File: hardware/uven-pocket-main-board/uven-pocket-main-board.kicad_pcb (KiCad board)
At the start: 4 copper layers, 120 x 56 mm, 78 parts, among them J1 Raspberry_Pi_2_3, J10 VDrive, J11 GND, J2 FAN, J3 TEMP_CHAMBER1, J4 TEMP_CHAMBER0, J5 1-282834-2, J6 VDrive, J7 GND, J8 VDrive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

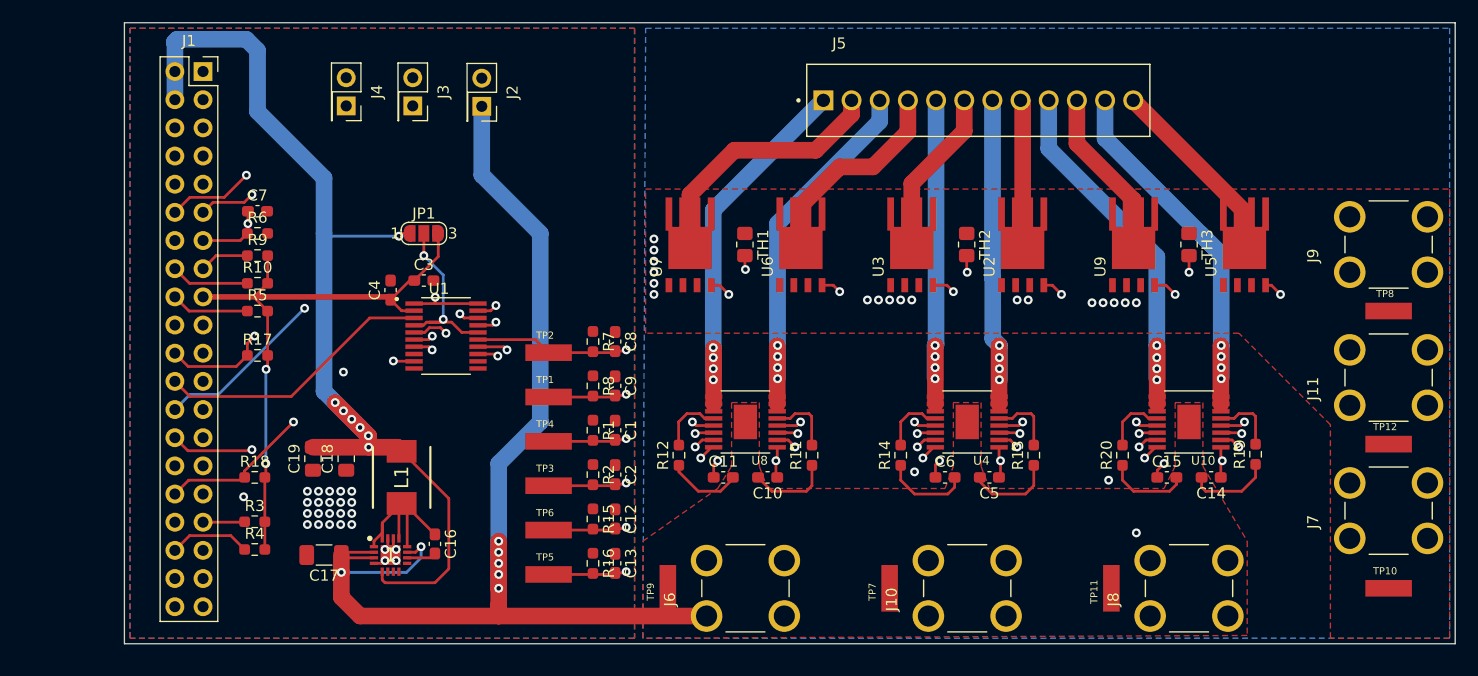
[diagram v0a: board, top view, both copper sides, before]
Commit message: single led copper base + uven pocket finished
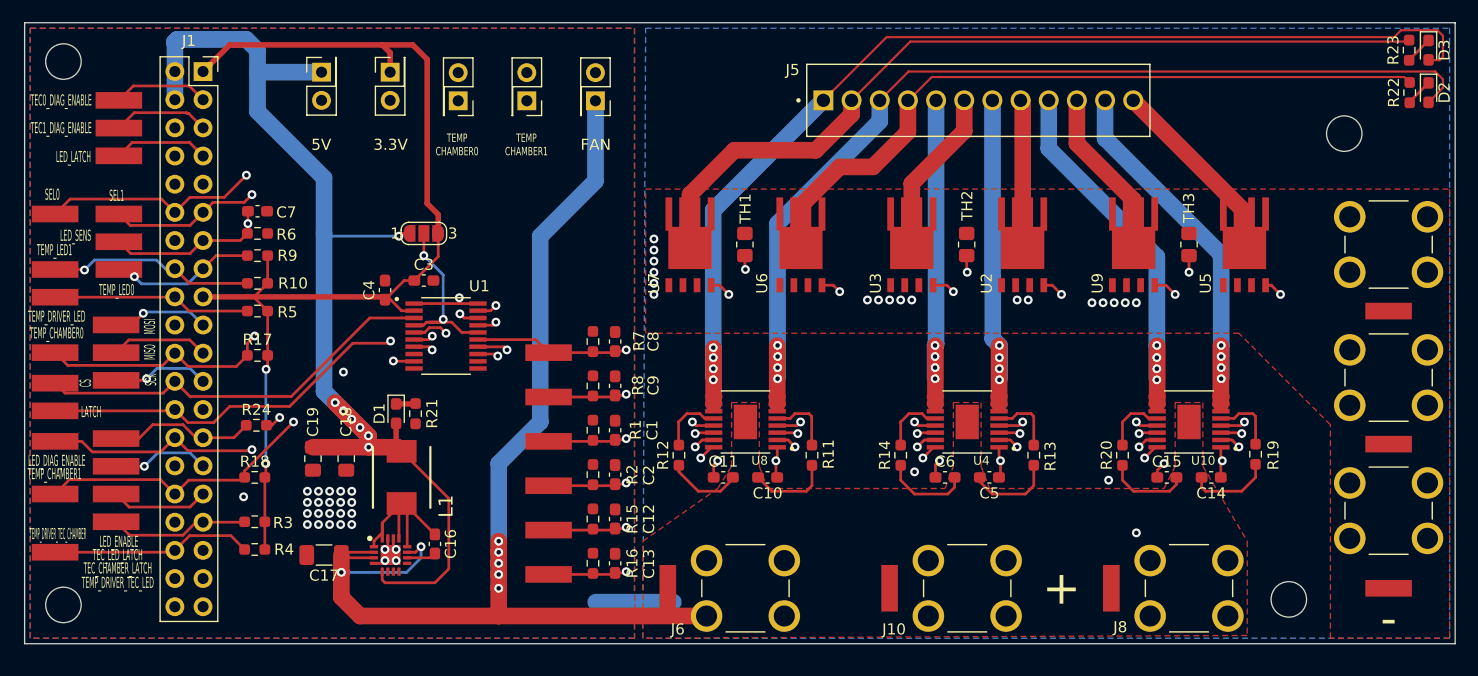
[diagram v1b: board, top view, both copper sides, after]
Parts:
- added D1: LED, LED_SMD:LED_0603_1608Metric_Pad1.05x0.95mm_HandSolder, F.Cu at (136.5, 92.2)
- added D2: LED, LED_SMD:LED_0603_1608Metric_Pad1.05x0.95mm_HandSolder, F.Cu at (229.6, 63.3)
- added D3: LED, LED_SMD:LED_0603_1608Metric_Pad1.05x0.95mm_HandSolder, F.Cu at (229.6, 59.5)
- added H1: MountingHole, MountingHole:MountingHole_3.2mm_M3, F.Cu at (217.0, 109.0)
- added H2: MountingHole, MountingHole:MountingHole_3.2mm_M3, F.Cu at (106.5, 109.5)
- added H3: MountingHole, MountingHole:MountingHole_3.2mm_M3, F.Cu at (106.5, 60.5)
- added H4: MountingHole, MountingHole:MountingHole_3.2mm_M3, F.Cu at (222.0, 67.0)
- added J12: 3.3V, Connector_PinSocket_2.54mm:PinSocket_2x01_P2.54mm_Vertical, F.Cu at (136.0, 61.5)
- added J13: 5V, Connector_PinSocket_2.54mm:PinSocket_2x01_P2.54mm_Vertical, F.Cu at (129.8, 61.5)
- added R21: 1K, Resistor_SMD:R_0603_1608Metric_Pad0.98x0.95mm_HandSolder, F.Cu at (138.2, 92.2)
- added R22: 10k, Resistor_SMD:R_0603_1608Metric_Pad0.98x0.95mm_HandSolder, F.Cu at (227.9, 63.3)
- added R23: 10k, Resistor_SMD:R_0603_1608Metric_Pad0.98x0.95mm_HandSolder, F.Cu at (227.8, 59.5)
- added R24: 10k, Resistor_SMD:R_0603_1608Metric_Pad0.98x0.95mm_HandSolder, F.Cu at (123.9, 93.3)
- added TP13: TEMP_DRIVER_LED, custom_lib:TP420X150, F.Cu at (105.8, 81.8)
- added TP14: TEMP_CHAMBER0, custom_lib:TP420X150, F.Cu at (105.8, 86.8)
- added TP15: LED_SENS, custom_lib:TP420X150, F.Cu at (111.5, 76.8)
- added TP16: TEMP_DRIVER_TEC_CHAMBER, custom_lib:TP420X150, F.Cu at (105.8, 104.8)
- added TP17: TEMP_LED0, custom_lib:TP420X150, F.Cu at (111.5, 79.2)
- added TP18: TEMP_LED1, custom_lib:TP420X150, F.Cu at (105.8, 79.2)
- added TP19: SEL1, custom_lib:TP420X150, F.Cu at (111.5, 74.2)
- added TP20: SEL0, custom_lib:TP420X150, F.Cu at (105.8, 74.2)
- added TP21: LATCH, custom_lib:TP420X150, F.Cu at (105.8, 92.0)
- added TP22: CS, custom_lib:TP420X150, F.Cu at (105.8, 89.5)
- added TP23: MISO, custom_lib:TP420X150, F.Cu at (111.2, 86.8)
- added TP24: MOSI, custom_lib:TP420X150, F.Cu at (111.2, 84.2)
- added TP25: SCK, custom_lib:TP420X150, F.Cu at (111.2, 89.2)
- added TP26: LED_ENABLE, custom_lib:TP420X150, F.Cu at (111.2, 94.5)
- added TP27: LED_DIAG_ENABLE, custom_lib:TP420X150, F.Cu at (105.8, 94.8)
- added TP28: TEC0_DIAG_ENABLE, custom_lib:TP420X150, F.Cu at (111.5, 64.0)
- added TP29: TEC1_DIAG_ENABLE, custom_lib:TP420X150, F.Cu at (111.5, 66.5)
- added TP30: LED_LATCH, custom_lib:TP420X150, F.Cu at (111.5, 69.0)
- added TP31: TEC_LED_LATCH, custom_lib:TP420X150, F.Cu at (111.2, 97.0)
- added TP32: TEC_CHAMBER_LATCH, custom_lib:TP420X150, F.Cu at (111.2, 99.5)
- added TP33: TEMP_CHAMBER1, custom_lib:TP420X150, F.Cu at (105.8, 99.5)
- added TP34: TEMP_DRIVER_TEC_LED, custom_lib:TP420X150, F.Cu at (111.2, 102.0)
- moved J3 10.3 mm to (148.3, 64.0)
- moved J2 10.3 mm to (154.5, 64.0)
- moved J4 10.1 mm to (142.1, 64.0)
- moved C4 0.50 mm to (135.5, 81.1)
- renumbered 1 to 11111
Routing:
- net /LED1+: track 34.1 -> 96.2 mm
- net /LED0+: track 34.1 -> 88.8 mm
- net /LED1-: track 23.6 -> 76.5 mm
- net /LED0-: track 19.1 -> 65.4 mm
- net +3.3V: track 59.8 -> 101.0 mm
- net /TEMP_CHAMBER0: track 33.6 -> 50.0 mm
- net /TEMP_CHAMBER1: track 48.2 -> 64.5 mm
- net /LED_ENABLE: track 85.4 -> 98.6 mm
- net /SEL0: track 123.0 -> 134.8 mm
- net /LED_DIAG_ENABLE: track 74.3 -> 86.0 mm
- net /CS: track 25.1 -> 36.7 mm
- net /LATCH: track 36.4 -> 48.0 mm
- net /TEMP_LED1: track 7.08 -> 18.6 mm, vias 0 -> 1
- net /TEMP_DRIVER_TEC_CHAMBER: track 160.7 -> 171.5 mm
- net /TEMP_DRIVER_LED: track 101.8 -> 112.6 mm
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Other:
- board size 120 x 56 mm -> 129 x 56 mm
- board text added: "+"
- board text added: "-"
- board text added: "3.3V"
- board text added: "5V"
- board text added: "CS"
- board text added: "FAN"
- board text added: "LATCH"
- board text added: "LED_DIAG_ENABLE"
- board text added: "LED_ENABLE"
- board text added: "LED_LATCH"
- board text added: "LED_SENS"
- board text added: "MISO"
- board text added: "MOSI"
- board text added: "SCK"
- board text added: "SEL0"
- board text added: "SEL1"
- board text added: "TEC0_DIAG_ENABLE"
- board text added: "TEC1_DIAG_ENABLE"
- board text added: "TEC_CHAMBER_LATCH"
- board text added: "TEC_LED_LATCH"
- board text added: "TEMP CHAMBER0"
- board text added: "TEMP CHAMBER1"
- board text added: "TEMP_CHAMBER0"
- board text added: "TEMP_CHAMBER1"
- board text added: "TEMP_DRIVER_LED"
- board text added: "TEMP_DRIVER_TEC_CHAMBER"
- board text added: "TEMP_DRIVER_TEC_LED"
- board text added: "TEMP_LED0"
- board text added: "TEMP_LED1"
